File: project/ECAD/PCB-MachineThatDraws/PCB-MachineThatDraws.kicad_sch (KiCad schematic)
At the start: 29 parts, among them J1 SD_Card_Device, J10 Conn_02x03_Odd_Even, J11 Conn_02x03_Odd_Even, J2 SDA/SCL/VCC/GND, J3 Switch, J4 Limit_Switch_X, J5 Moteur, J6 Moteur, J7 Barrel_Jack_Switch, J8 Screw_Terminal_01x02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

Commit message: pcb up
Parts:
- J4: footprint Connector_JST:JST_PH_B3B-PH-K_1x03_P2.00mm_Vertical -> Connector_PinHeader_2.54mm:PinHeader_1x03_P2.54mm_Vertical
- J9: footprint Connector:FanPinHeader_1x03_P2.54mm_Vertical -> Connector_PinHeader_2.54mm:PinHeader_1x03_P2.54mm_Vertical

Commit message: pcb up
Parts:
- J3: footprint Connector_JST:JST_PH_B3B-PH-K_1x03_P2.00mm_Vertical -> Connector_PinHeader_2.54mm:PinHeader_1x03_P2.54mm_Vertical
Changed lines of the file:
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@@
 			)
 		)
-		(property "Footprint" "Connector_JST:JST_PH_B3B-PH-K_1x03_P2.00mm_Vertical"
+		(property "Footprint" "Connector_PinHeader_2.54mm:PinHeader_1x03_P2.54mm_Vertical"
 			(at 26.67 106.68 0)
 			(hide yes)

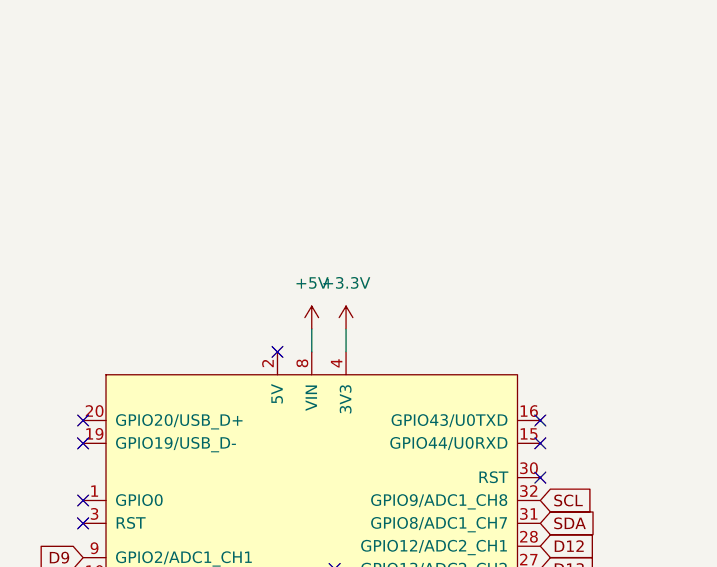
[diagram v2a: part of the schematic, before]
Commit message: pcb + sch up
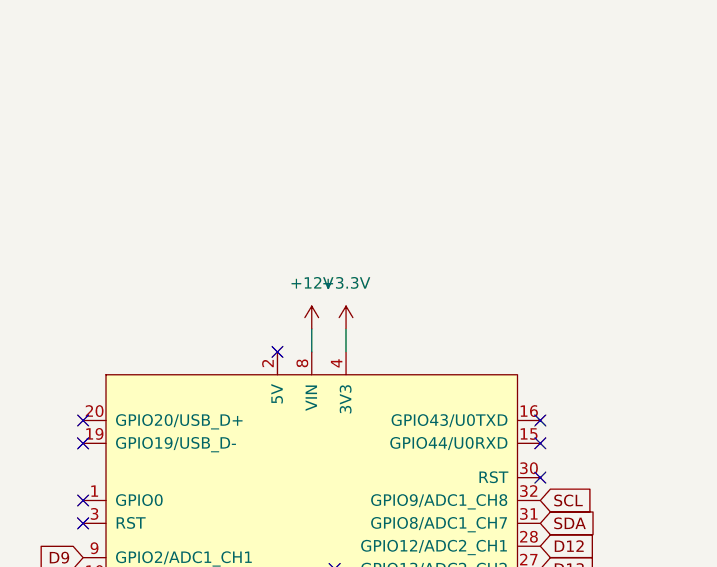
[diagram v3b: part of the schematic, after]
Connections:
- net +12V: now also U1.8 (VIN)
- net +5V: no longer U1.8 (VIN)
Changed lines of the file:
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@@
+	)
+	(symbol
+		(lib_id "power:+5V")
+		(at 46.99 20.32 0)
+		(unit 1)
+		(body_style 1)
+		(exclude_from_sim no)
+		(in_bom yes)
+		(on_board yes)
+		(in_pos_files yes)
+		(dnp no)
+		(fields_autoplaced yes)
+		(property "Reference" "#PWR034"
+			(at 46.99 24.13 0)
+			(hide yes)
+			(show_name no)
+			(do_not_autoplace no)
+			(effects
+				(font
+					(size 1.27 1.27)
+				)
+			)
+		)
+		(property "Value" "+12V"
+			(at 46.99 15.24 0)
+			(show_name no)
+			(do_not_autoplace no)
+			(effects
+				(font
+					(size 1.27 1.27)
+				)
+			)
+		)
+		(property "Footprint" ""
+			(at 46.99 20.32 0)
+			(hide yes)
+			(show_name no)
+			(do_not_autoplace no)
+			(effects
+				(font
+					(size 1.27 1.27)
+				)
+			)
+		)
+		(property "Datasheet" ""
+			(at 46.99 20.32 0)
+			(hide yes)
+			(show_name no)
+			(do_not_autoplace no)
+			(effects
+				(font
+					(size 1.27 1.27)
+				)
+			)
+		)
+		(property "Description" "Power symbol creates a global label with name \"+5V\""
+			(at 46.99 20.32 0)
+			(hide yes)
+			(show_name no)
+			(do_not_autoplace no)
+			(effects
+				(font
+					(size 1.27 1.27)
+				)
+			)
+		)
+		(pin "1"
+		)
+		(instances
+			(project "PCB-MachineThatDraws"
+				(path "/d1309c4d-f5c5-4ae1-9a0a-1ebc6300afdd"
+					(reference "#PWR034")
+					(unit 1)
+				)
+			)
+		)
 	)
 	(symbol
@@
 					(unit 1)
 				)
-			)
-		)
-	)
-	(symbol
-		(lib_id "power:+5V")
-		(at 46.99 20.32 0)
-		(unit 1)
-		(body_style 1)
-		(exclude_from_sim no)
-		(in_bom yes)
-		(on_board yes)
-		(in_pos_files yes)
-		(dnp no)
-		(fields_autoplaced yes)
-		(property "Reference" "#PWR03"
-			(at 46.99 24.13 0)
-			(hide yes)
-			(show_name no)
-			(do_not_autoplace no)
-			(effects
-				(font
-					(size 1.27 1.27)
-				)
-			)
-		)
-		(property "Value" "+5V"
-			(at 46.99 15.24 0)
-			(show_name no)
-			(do_not_autoplace no)
-			(effects
-				(font
-					(size 1.27 1.27)
-				)
-			)
-		)
-		(property "Footprint" ""
-			(at 46.99 20.32 0)
-			(hide yes)
-			(show_name no)
-			(do_not_autoplace no)
-			(effects
-				(font
-					(size 1.27 1.27)
-				)
-			)
-		)
-		(property "Datasheet" ""
-			(at 46.99 20.32 0)
-			(hide yes)
-			(show_name no)
-			(do_not_autoplace no)
-			(effects
-				(font
-					(size 1.27 1.27)
-				)
-			)
-		)
-		(property "Description" "Power symbol creates a global label with name \"+5V\""
-			(at 46.99 20.32 0)
-			(hide yes)
-			(show_name no)
-			(do_not_autoplace no)
-			(effects
-				(font
-					(size 1.27 1.27)
-				)
-			)
-		)
-		(pin "1"
-		)
-		(instances
-			(project "PCB-MachineThatDraws"
-				(path "/d1309c4d-f5c5-4ae1-9a0a-1ebc6300afdd"
-					(reference "#PWR03")
-					(unit 1)
-				)

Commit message: pcb correction
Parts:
- J5, J6: footprint Connector:NS-Tech_Grove_1x04_P2mm_Vertical -> Connector_PinHeader_2.54mm:PinHeader_1x04_P2.54mm_Vertical
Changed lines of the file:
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@@
 			)
 		)
-		(property "Footprint" "Connector:NS-Tech_Grove_1x04_P2mm_Vertical"
+		(property "Footprint" "Connector_PinHeader_2.54mm:PinHeader_1x04_P2.54mm_Vertical"
 			(at 200.66 125.73 0)
 			(hide yes)
@@
 			)
 		)
-		(property "Footprint" "Connector:NS-Tech_Grove_1x04_P2mm_Vertical"
+		(property "Footprint" "Connector_PinHeader_2.54mm:PinHeader_1x04_P2.54mm_Vertical"
 			(at 261.62 127 0)
 			(hide yes)
